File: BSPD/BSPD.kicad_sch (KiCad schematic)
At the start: 41 parts, among them J1 DT13-48PABCD-R015, K1 Latching Relay, Q1 STS6NF20V, Q2 STS6NF20V, Q3 STS6NF20V, U1 LM7805CT, U10 DK1A1B-12V, U12 LM555N, U13 LM7805CT, U2 NSL-32, U2 OP AMP, U3 OP AMP, U4 Inverter (Not Gate), U5 2x4 OR GATE, U6 LM555N, U8 NAND, U9 AND GATE

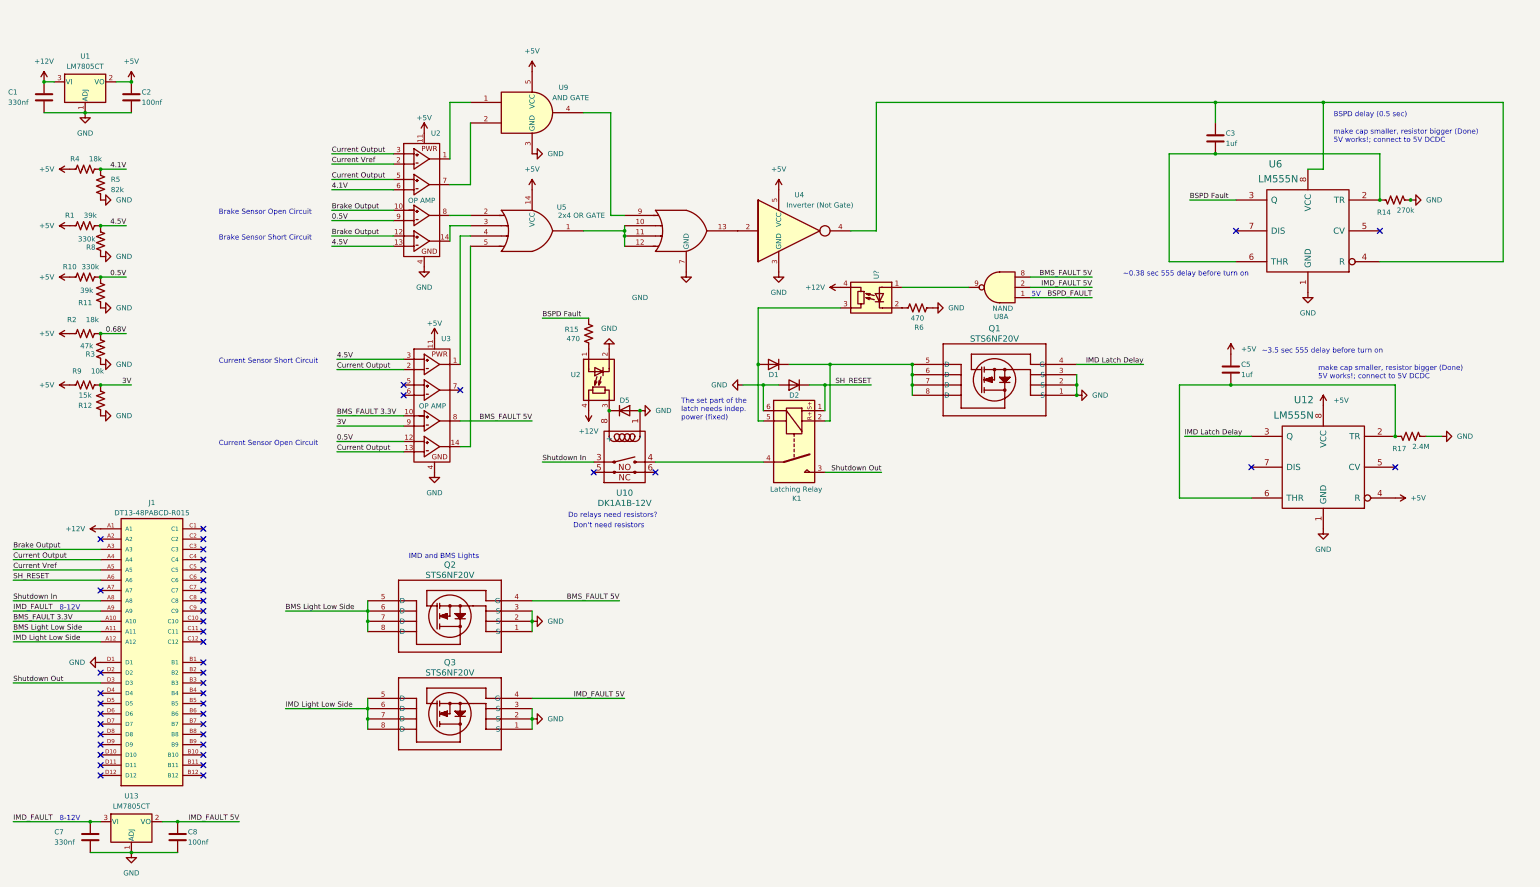
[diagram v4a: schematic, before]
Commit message: Updated timer and connections
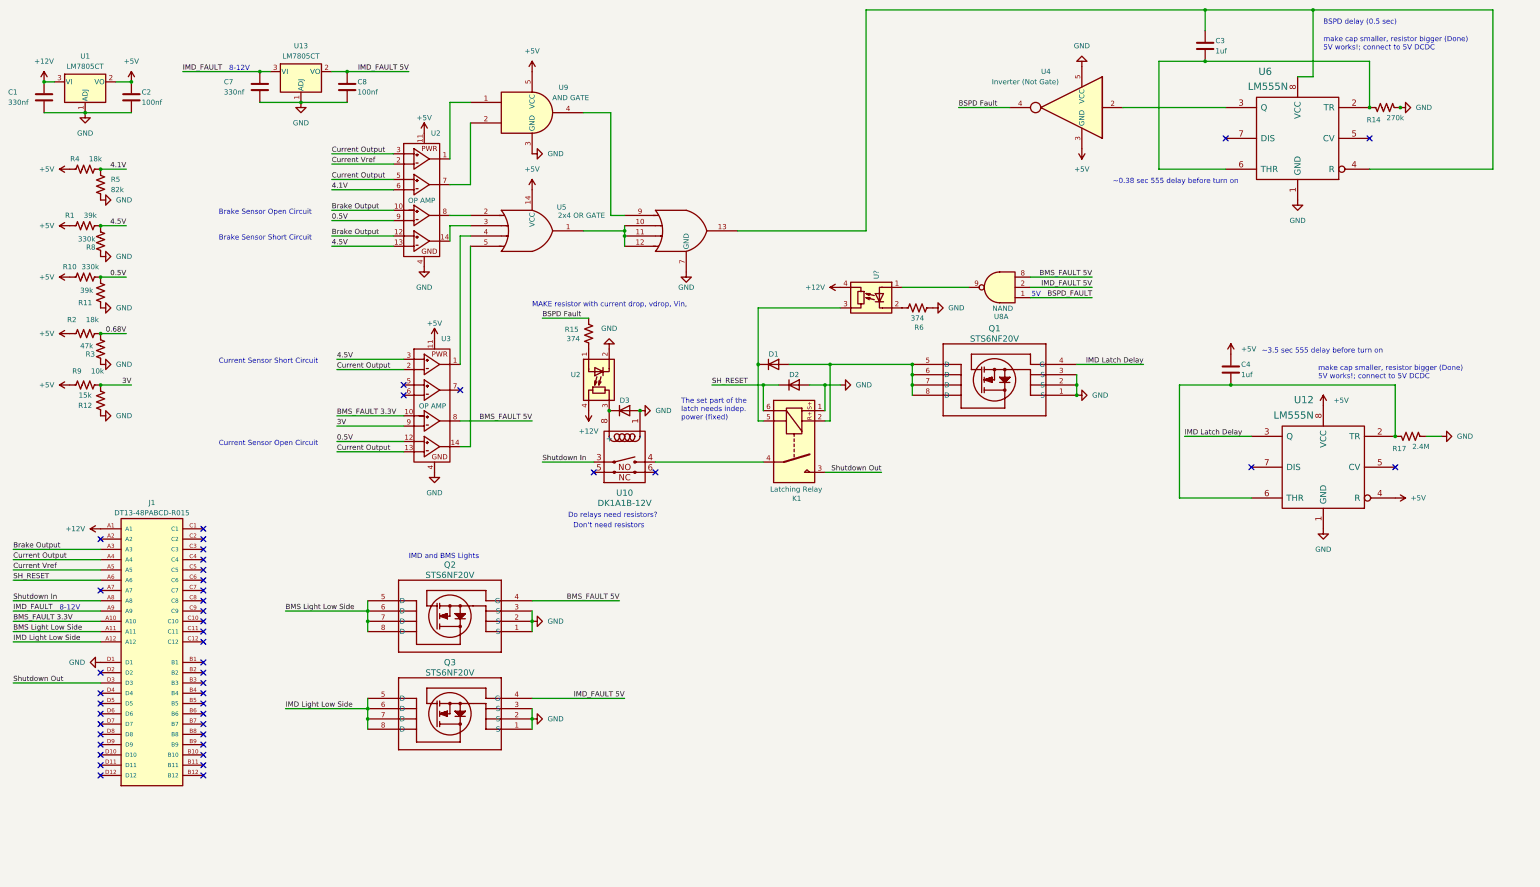
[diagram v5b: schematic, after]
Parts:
- removed C5: 1uf, symbol Device:C
- removed D5: D, Diode_THT:D_DO-41_SOD81_P10.16mm_Horizontal, symbol Device:D
- added C4: 1uf, Capacitor_SMD:C_0805_2012Metric_Pad1.18x1.45mm_HandSolder, symbol Device:C
- added D3: D, Diode_SMD:D_2010_5025Metric_Pad1.52x2.65mm_HandSolder, symbol Device:D
- C1, C2, C3, C7, C8: footprint (none) -> Capacitor_SMD:C_0805_2012Metric_Pad1.18x1.45mm_HandSolder
- D1, D2: footprint (none) -> Diode_SMD:D_2010_5025Metric_Pad1.52x2.65mm_HandSolder
- R15, R6: value 470 -> 374
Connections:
- net +5V: now also U4.3 (GND), C4.1; no longer U4.5 (VCC)
- net BSPD Fault: now also U4.4; no longer U6.3 (Q)
- net GND: now also K1.1, U4.5 (VCC), D3.2 (A); no longer K1.6, U4.3 (GND)
- net SH_RESET: now also K1.6; no longer K1.1
- net at C3.1, U6.4 (R), U6.8 (VCC): now also U5.13; no longer U4.4
- net at U10.8 (+), U2.3 (R): now also D3.1 (K)
- net at K1.2, Q1.5 (D), Q1.6 (D)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: now also D1.2 (A); no longer D1.1 (K)
- net at K1.5, U?.3 (R): now also D1.1 (K); no longer D1.2 (A)
- net at U4.2: now also U6.3 (Q); no longer U5.13
- net at R17.1, U12.2 (TR), U12.6 (THR): now also C4.2
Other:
- note added: "MAKE resistor with current drop, vdrop, Vin,"
- moved on the sheet: C3, C7, C8, D1, R14, U13, U4, U6

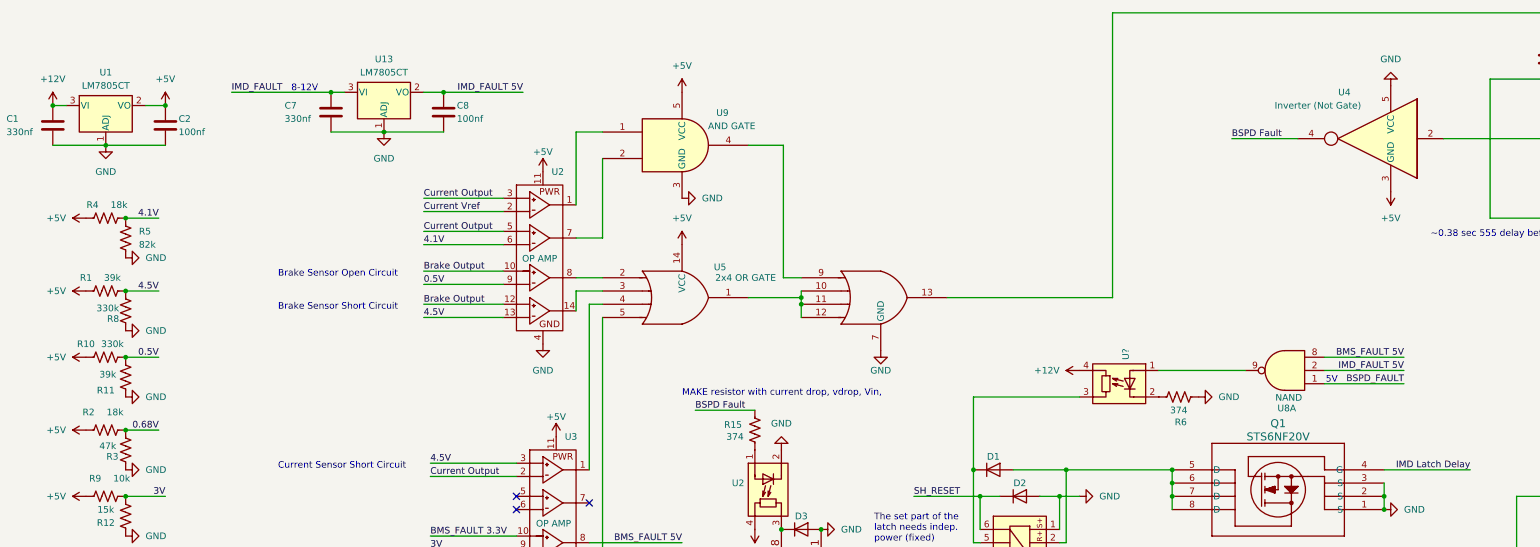
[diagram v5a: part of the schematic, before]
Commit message: finished shutdown circuitry
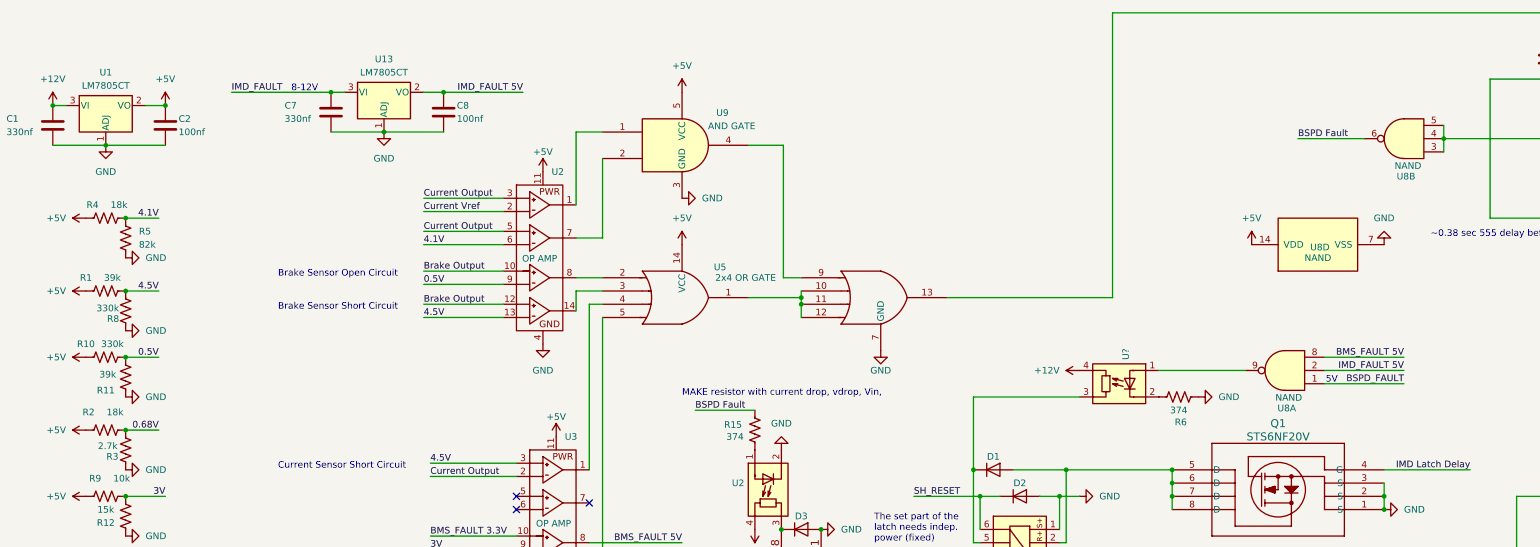
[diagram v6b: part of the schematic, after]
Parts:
- removed U4: Inverter (Not Gate), Package_SO:TSSOP-14_4.4x5mm_P0.65mm, symbol 74xGxx:74LVC1GU04DRL
- added unit 2 of U8
- added unit 4 of U8
- R3: value 47k -> 2.7k
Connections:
- net +5V: now also U8.14 (VDD)
- net BSPD Fault: now also U8.6
- net GND: now also U8.7 (VSS)
- net at U6.3 (Q): now also U8.3, U8.4, U8.5
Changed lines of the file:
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@@
   (junction (at 311.15 29.21) (diameter 0) (color 0 0 0 0)
+  )
+  (junction (at 290.83 40.64) (diameter 0) (color 0 0 0 0)
   )
   (junction (at 38.1 96.52) (diameter 0) (color 0 0 0 0)
@@
     (stroke (width 0) (type default))
   )
+  (wire (pts (xy 290.83 40.64) (xy 290.83 43.18))
+    (stroke (width 0) (type default))
+  )
   (wire (pts (xy 129.54 124.46) (xy 127 124.46))
     (stroke (width 0) (type default))
@@
     (stroke (width 0) (type default))
   )
+  (wire (pts (xy 290.83 38.1) (xy 290.83 40.64))
+    (stroke (width 0) (type default))
+  )
   (wire (pts (xy 95.25 68.58) (xy 110.49 68.58))
     (stroke (width 0) (type default))
@@
     (stroke (width 0) (type default))
   )
-  (wire (pts (xy 250.19 40.64) (xy 262.89 40.64))
+  (wire (pts (xy 262.89 40.64) (xy 275.59 40.64))
     (stroke (width 0) (type default))
   )
@@
     (effects (font (size 1.27 1.27)) (justify left bottom))
   )
-  (label "BSPD Fault" (at 250.19 40.64 0) (fields_autoplaced)
+  (label "BSPD Fault" (at 262.89 40.64 0) (fields_autoplaced)
     (effects (font (size 1.27 1.27)) (justify left bottom))
   )
@@
     )
   )
-  (symbol (lib_id "power:GND") (at 280.67 30.48 180) (unit 1)
-    (in_bom yes) (on_board yes) (dnp no) (fields_autoplaced)
-    (property "Reference" "#PWR017" (at 280.67 24.13 0)
-      (effects (font (size 1.27 1.27)) hide)
-    )
-    (property "Value" "GND" (at 280.67 25.4 0)
-      (effects (font (size 1.27 1.27)))
-    )
-    (property "Footprint" "" (at 280.67 30.48 0)
-      (effects (font (size 1.27 1.27)) hide)
-    )
-    (property "Datasheet" "" (at 280.67 30.48 0)
+  (symbol (lib_id "power:GND") (at 279.4 60.96 180) (unit 1)
+    (in_bom yes) (on_board yes) (dnp no) (fields_autoplaced)
+    (property "Reference" "#PWR017" (at 279.4 54.61 0)
+      (effects (font (size 1.27 1.27)) hide)
+    )
+    (property "Value" "GND" (at 279.4 55.88 0)
+      (effects (font (size 1.27 1.27)))
+    )
+    (property "Footprint" "" (at 279.4 60.96 0)
+      (effects (font (size 1.27 1.27)) hide)
+    )
+    (property "Datasheet" "" (at 279.4 60.96 0)
       (effects (font (size 1.27 1.27)) hide)
     )
@@
     )
   )
-  (symbol (lib_id "74xGxx:74LVC1GU04DRL") (at 280.67 40.64 0) (mirror y) (unit 1)
-    (in_bom yes) (on_board yes) (dnp no)
-    (property "Reference" "U4" (at 271.78 31.75 0)
-      (effects (font (size 1.27 1.27)))
-    )
-    (property "Value" "Inverter (Not Gate)" (at 266.7 34.29 0)
-      (effects (font (size 1.27 1.27)))
-    )
-    (property "Footprint" "Package_SO:TSSOP-14_4.4x5mm_P0.65mm" (at 280.67 53.34 0)
-      (effects (font (size 1.27 1.27)) hide)
-    )
-    (property "Datasheet" "http://www.ti.com/lit/ds/symlink/sn74lvc1gu04.pdf" (at 284.48 40.64 0)
-      (effects (font (size 1.27 1.27)) hide)
-    )
-    (pin "1")
-    (pin "2")
-    (pin "3")
-    (pin "4")
-    (pin "5")
-    (instances
-      (project "BSPD"
-        (path "/9b958334-fa88-4811-8197-71444a07b1b5"
-          (reference "U4") (unit 1)
-        )
-      )
-    )
-  )
   (symbol (lib_id "power:GND") (at 118.11 80.01 0) (unit 1)
     (in_bom yes) (on_board yes) (dnp no) (fields_autoplaced)
@@
     )
   )
-  (symbol (lib_id "power:+5V") (at 280.67 50.8 180) (unit 1)
-    (in_bom yes) (on_board yes) (dnp no) (fields_autoplaced)
-    (property "Reference" "#PWR013" (at 280.67 46.99 0)
-      (effects (font (size 1.27 1.27)) hide)
-    )
-    (property "Value" "+5V" (at 280.67 55.88 0)
-      (effects (font (size 1.27 1.27)))
-    )
-    (property "Footprint" "" (at 280.67 50.8 0)
-      (effects (font (size 1.27 1.27)) hide)
-    )
-    (property "Datasheet" "" (at 280.67 50.8 0)
+  (symbol (lib_id "power:+5V") (at 254 60.96 0) (unit 1)
+    (in_bom yes) (on_board yes) (dnp no) (fields_autoplaced)
+    (property "Reference" "#PWR013" (at 254 64.77 0)
+      (effects (font (size 1.27 1.27)) hide)
+    )
+    (property "Value" "+5V" (at 254 55.88 0)
+      (effects (font (size 1.27 1.27)))
+    )
+    (property "Footprint" "" (at 254 60.96 0)
+      (effects (font (size 1.27 1.27)) hide)
+    )
+    (property "Datasheet" "" (at 254 60.96 0)
       (effects (font (size 1.27 1.27)) hide)
     )
@@
     )
   )
+  (symbol (lib_id "4xxx:4023") (at 283.21 40.64 180) (unit 2)
+    (in_bom yes) (on_board yes) (dnp no)
+    (property "Reference" "U8" (at 283.591 47.879 0)
+      (effects (font (size 1.27 1.27)))
+    )
+    (property "Value" "NAND" (at 283.972 45.847 0)
+      (effects (font (size 1.27 1.27)))
+    )
+    (property "Footprint" "Package_DIP:DIP-14_W7.62mm" (at 283.21 40.64 0)
+      (effects (font (size 1.27 1.27)) hide)
+    )
+    (property "Datasheet" "http://www.intersil.com/content/dam/Intersil/documents/cd40/cd4011bms-12bms-23bms.pdf" (at 283.21 40.64 0)
+      (effects (font (size 1.27 1.27)) hide)
+    )
+    (pin "1")
+    (pin "2")
+    (pin "8")
+    (pin "9")
+    (pin "3")
+    (pin "4")
+    (pin "5")
+    (pin "6")
+    (pin "10")
+    (pin "11")
+    (pin "12")
+    (pin "13")
+    (pin "14")
+    (pin "7")
+    (instances
+      (project "BSPD"
+        (path "/9b958334-fa88-4811-8197-71444a07b1b5"
+          (reference "U8") (unit 2)
+        )
+      )
+      (project "Acc_Board"
+        (path "/e19d26dd-723b-45e6-9d59-b1730158e759"
+          (reference "U5") (unit 1)
+        )
+      )
+    )
+  )
   (symbol (lib_id "power:+5V") (at 30.48 69.85 90) (unit 1)
     (in_bom yes) (on_board yes) (dnp no) (fields_autoplaced)
@@
         (path "/9b958334-fa88-4811-8197-71444a07b1b5"
           (reference "#PWR025") (unit 1)
+        )
+      )
+    )
+  )
+  (symbol (lib_id "4xxx:4023") (at 266.7 60.96 90) (unit 4)
+    (in_bom yes) (on_board yes) (dnp no)
+    (property "Reference" "U8" (at 267.081 61.468 90)
+      (effects (font (size 1.27 1.27)))
+    )
+    (property "Value" "NAND" (at 266.7 63.5 90)
+      (effects (font (size 1.27 1.27)))
+    )
+    (property "Footprint" "Package_DIP:DIP-14_W7.62mm" (at 266.7 60.96 0)
+      (effects (font (size 1.27 1.27)) hide)
+    )
+    (property "Datasheet" "http://www.intersil.com/content/dam/Intersil/documents/cd40/cd4011bms-12bms-23bms.pdf" (at 266.7 60.96 0)
+      (effects (font (size 1.27 1.27)) hide)
+    )
+    (pin "1")
+    (pin "2")
+    (pin "8")
+    (pin "9")
+    (pin "3")
+    (pin "4")
+    (pin "5")
+    (pin "6")
+    (pin "10")
+    (pin "11")
+    (pin "12")
+    (pin "13")
+    (pin "14")
+    (pin "7")
+    (instances
+      (project "BSPD"
+        (path "/9b958334-fa88-4811-8197-71444a07b1b5"
+          (reference "U8") (unit 4)
+        )
+      )
+      (project "Acc_Board"
+        (path "/e19d26dd-723b-45e6-9d59-b1730158e759"
+          (reference "U5") (unit 1)
         )
       )
@@
       (effects (font (size 1.27 1.27)))
     )
-    (property "Value" "47k" (at 34.671 99.568 0)
-      (effects (font (size 1.27 1.27)))
-    )
+    (property "Value" "2.7k" (at 34.671 99.568 0)
+      (effects (font (size 1.27 1.27)))
+    )
